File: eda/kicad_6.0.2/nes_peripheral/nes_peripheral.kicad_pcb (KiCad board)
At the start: 2 copper layers, 100 x 100 mm, 111 parts, among them J1 CONN_USER, J11 CONN_JOY2_OE_SEL, J12 CONN_JOY1_OE_SEL, J15 CONN_JOY1_MIC, J16 CONN_5V_RESERVE, J2 CONN_JOY1_FC_COMPATIBLE, J22 CONN_JOY2_MIC, J23 FC_CONN, J24 CONN_CART_DBG, J25 CONN_CART_DBG, J28 CONN_JOY2_DBGSEL, J29 CONN_JOY1_DBGSEL, J3 CONN_JOY2_FC_COMPATIBLE, J30 CONN_GAINSEL, J31 Screw_Terminal_SPK, J33 CONN_JOY2_DBG, J34 CONN_JOY1_DBG, J4 Jack_EXT5V, J7 CONN_CART_OE_SEL, J8 CONN_5VSEL, U1 TXB0104PW, U10 TXB0104PW, U11 TXB0104PW, U12 TXB0104PW, U13 TXB0104PW, U14 TXB0104PW, U15 TXB0104PW, U16 TXB0104PW, U17 4021, U18 4021, U19 MAX98357, U2 TXB0104PW, U3 TXB0104PW, U4 TXB0104PW, U5 TXB0104PW, U6 TXB0104PW, U7 TXB0104PW, U8 TXB0104PW, U9 TXB0104PW

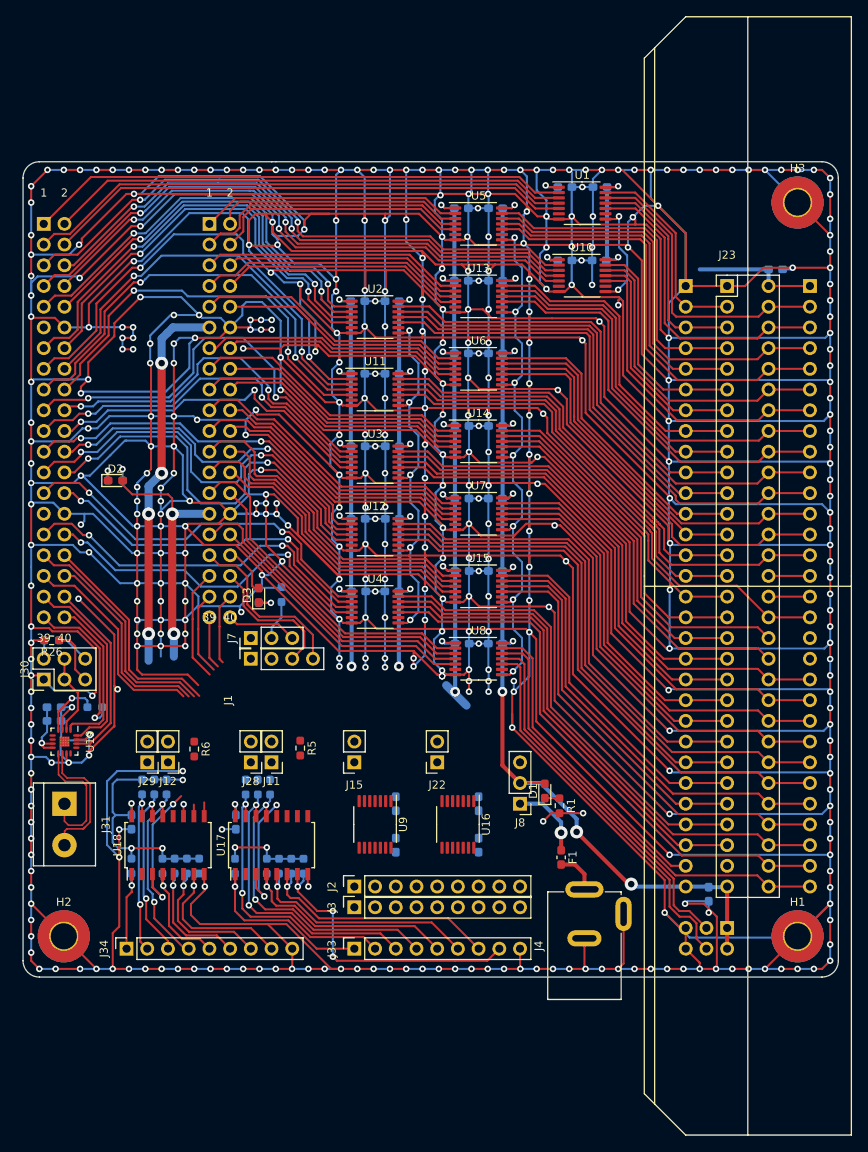
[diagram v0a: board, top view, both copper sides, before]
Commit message: feat: コントローラ用回路を引いた
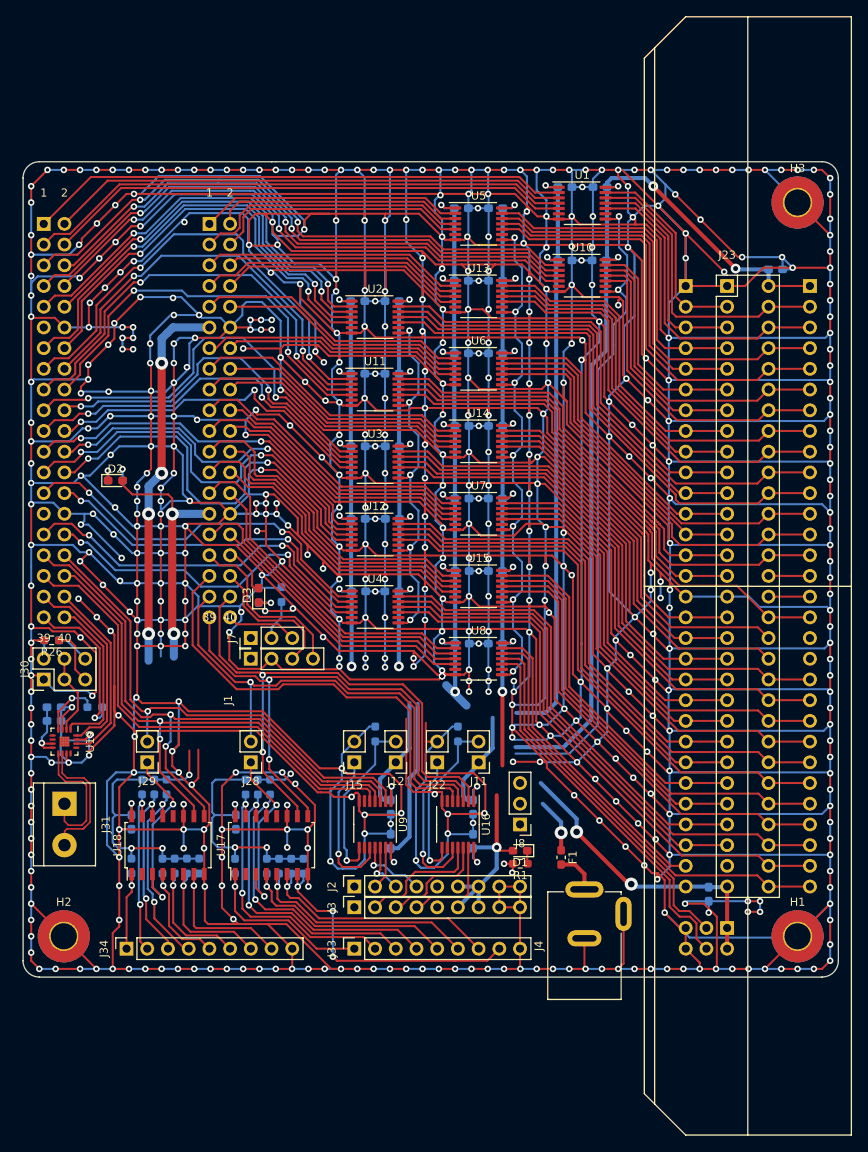
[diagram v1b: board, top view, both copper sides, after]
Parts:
- R5, R6: moved to B.Cu
- moved J12 27.9 mm to (86.4, 116.8)
- moved J11 25.4 mm to (96.5, 116.8)
- moved R6 22.3 mm to (83.8, 113.4), turned to 90 degrees
- moved R5 19.4 mm to (94.0, 113.4), turned to 90 degrees
- moved R1 8.59 mm to (101.6, 129.3), turned to 180 degrees
- moved D1 7.93 mm to (101.6, 127.7), turned to 180 degrees
- moved J8 2.54 mm to (101.6, 124.5)
- moved C33 0.83 mm to (95.8, 126.5)
- moved C28 0.80 mm to (95.8, 122.3)
- moved C21 0.79 mm to (85.7, 126.5)
- moved C13 0.75 mm to (85.7, 122.3)
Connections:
- JP2 pad 35: /3V3_JOY2_DO -> /3V3_JOY2_MICIN
- JP2 pad 37: /3V3_JOY2_MICIN -> /3V3_JOY2_DO
- U16 pad 11: /5V_JOY2_CLK -> /5V_JOY2_DO
- U16 pad 13: /5V_JOY2_DO -> /5V_JOY2_CLK
- U16 pad 2: /3V3_JOY2_DO -> /3V3_JOY2_CLK
- U16 pad 4: /3V3_JOY2_CLK -> /3V3_JOY2_DO
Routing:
- net GND: track 3216.7 -> 3973.7 mm, vias 458 -> 603
- net +3V3: track 244.9 -> 375.3 mm, vias 26 -> 29
- net +5V: track 226.5 -> 355.4 mm, vias 18 -> 23
- net /CART_OE: track 134.2 -> 201.0 mm
- net /3V3_JOY2_CLK: track 8.76 -> 71.1 mm, vias 0 -> 2
- net /3V3_JOY2_P/~{S}: track 6.45 -> 67.8 mm, vias 0 -> 2
- net /3V3_JOY2_DO: track 13.8 -> 60.1 mm, vias 0 -> 1
- net /3V3_JOY2_MICIN: track 10.3 -> 55.5 mm
- net /3V3_JOY1_P/~{S}: track 30.9 -> 75.2 mm, vias 0 -> 2
- net /3V3_JOY1_CLK: track 26.3 -> 69.4 mm, vias 0 -> 2
- net /3V3_JOY1_DO: track 27.3 -> 62.4 mm, vias 0 -> 1
- net /3V3_JOY1_RESERVE: track 26.5 -> 57.9 mm
- net /JOY1_OE_5V: track 0.00 -> 21.8 mm, vias 0 -> 1
- net /JOY2_OE_5V: track 0.00 -> 21.6 mm, vias 0 -> 1
- net /5V_JOY1_RESERVE: track 0.00 -> 18.9 mm, vias 0 -> 1
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
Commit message: feat: 3.3Vを配線
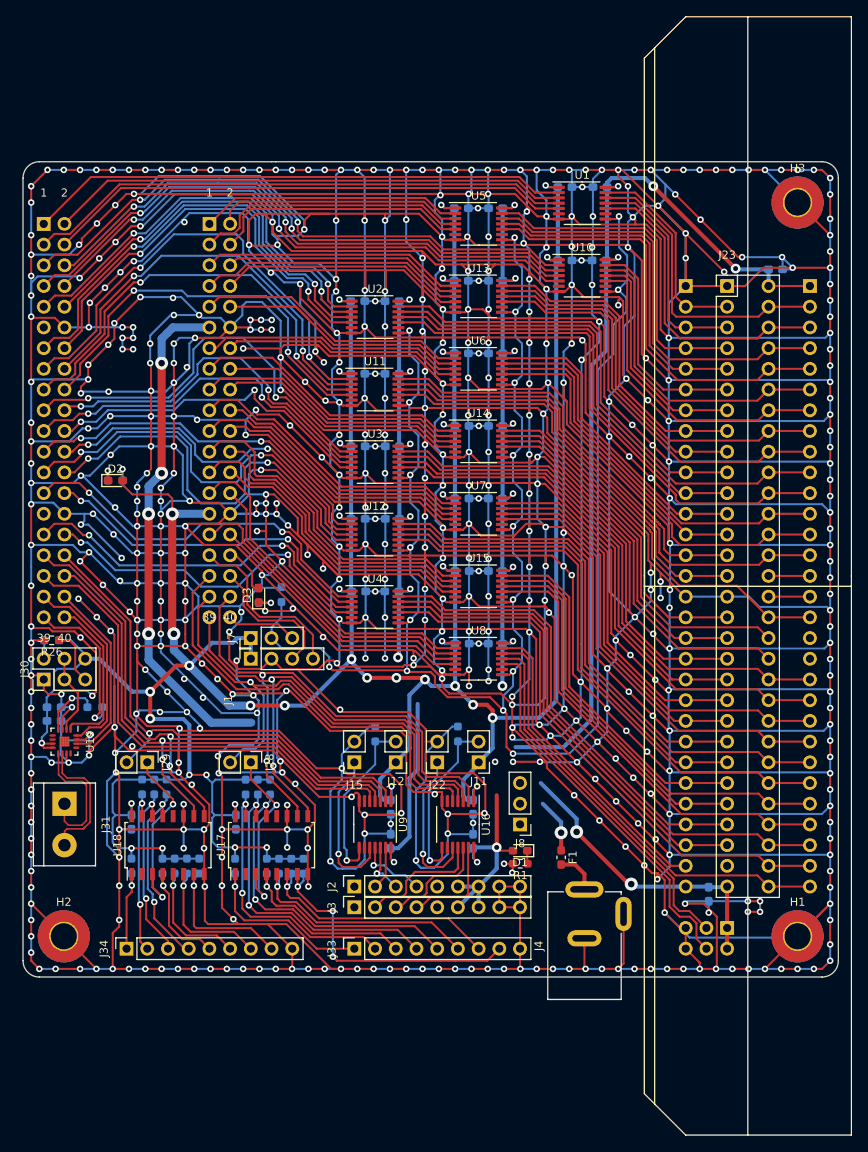
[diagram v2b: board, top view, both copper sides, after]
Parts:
- turned J28 to -90 degrees
- turned J29 to -90 degrees
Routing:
- net GND: track 3973.7 -> 4091.8 mm, vias 603 -> 615
- net +3V3: track 375.3 -> 473.1 mm, vias 29 -> 39
- net /CART_OE: track 201.0 -> 252.2 mm, vias 14 -> 18
- net /BOARD_5V: track 46.8 -> 62.5 mm
- net +5V: track 355.4 -> 344.6 mm
- net /3V3_JOY2_DO: track 60.1 -> 63.9 mm
- net /3V3_JOY1_DO: track 62.4 -> 64.6 mm
- net /3V3_JOY2_CLK: track 71.1 -> 69.0 mm
- net /3V3_JOY2_P/~{S}: track 67.8 -> 65.7 mm
- net /3V3_JOY2_MICIN: track 55.5 -> 53.7 mm
- net /3V3_JOY1_P/~{S}: track 75.2 -> 73.5 mm
- net /3V3_JOY1_RESERVE: track 57.9 -> 59.1 mm
- net /3V3_JOY1_CLK: track 69.4 -> 68.3 mm

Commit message: feat: 配線終わり
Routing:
- net GND: track 4091.8 -> 4256.6 mm, vias 615 -> 692
- net /BOARD_5V: track 62.5 -> 104.7 mm, vias 4 -> 7
- net +5V: track 344.6 -> 382.8 mm, vias 23 -> 25
- net /5V_~{VRAMCS}: track 47.2 -> 52.3 mm
- net /5V_~{PA13}: track 48.0 -> 53.1 mm
- net /5V_PD3: track 38.6 -> 43.6 mm
- net +3V3: track 473.1 -> 474.6 mm, vias 39 -> 35
- net /DAC_I2S_DIN: track 20.6 -> 20.0 mm
- net /5V_JOY2_CLK: track 13.2 -> 12.7 mm
- added copper zone on B.Cu, net GND
- added copper zone on F.Cu, net GND

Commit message: feat: DRC通した
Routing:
- net GND: track 4256.6 -> 4263.4 mm
- net +3V3: track 474.6 -> 475.2 mm
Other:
- board text removed: "39"
- board text removed: "40"

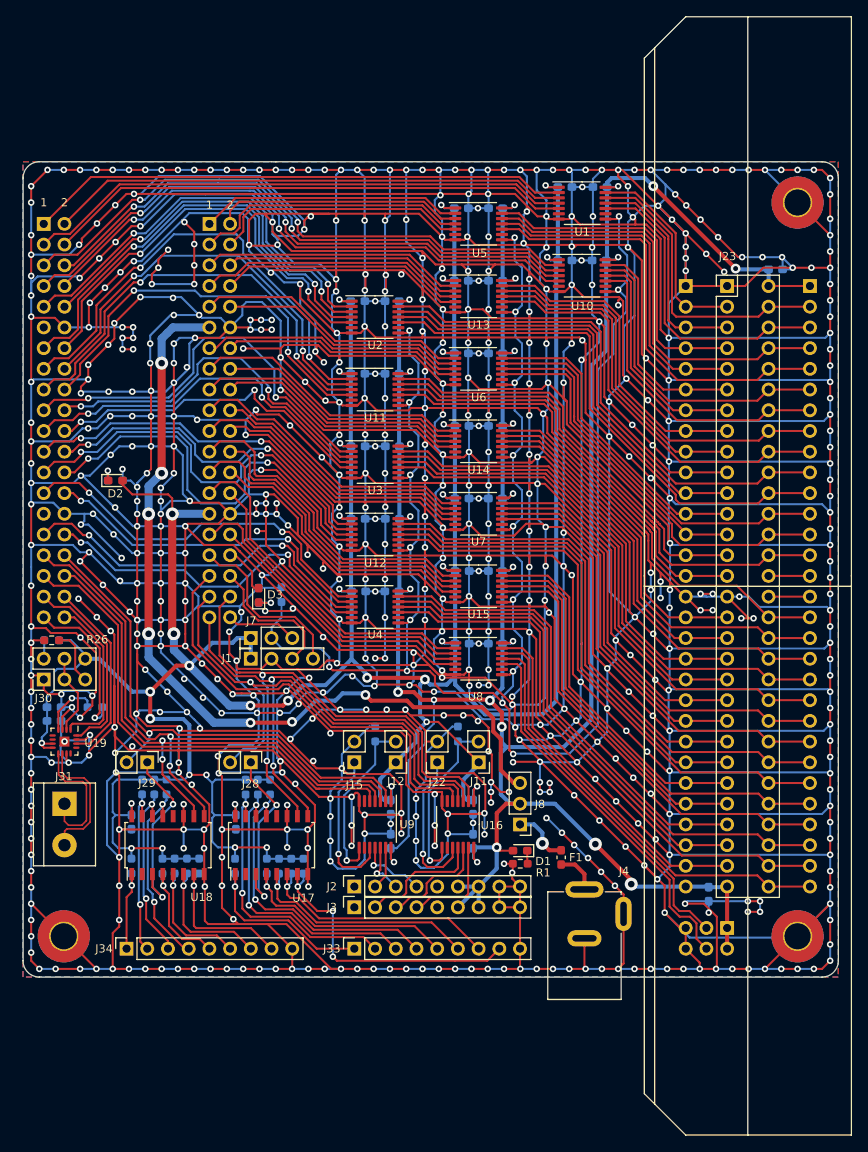
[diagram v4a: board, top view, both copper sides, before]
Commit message: feat: 表面のシルクを整備
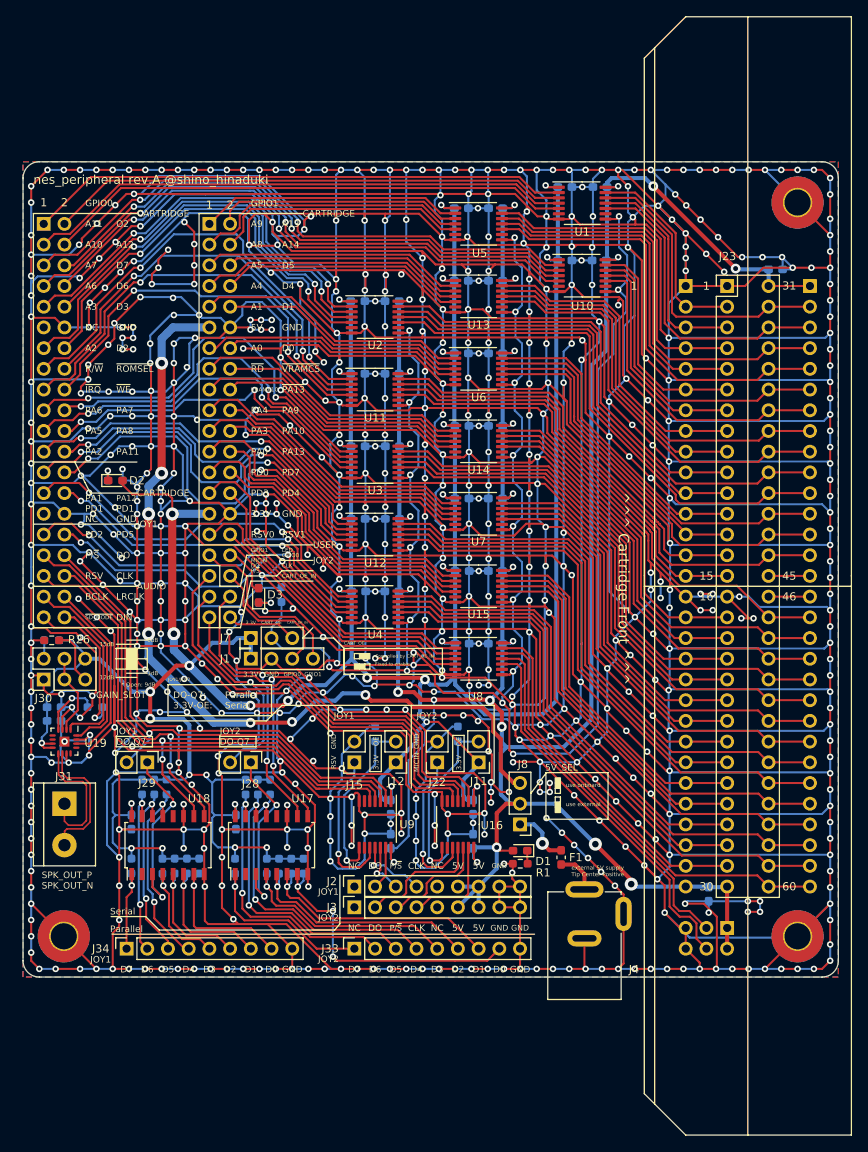
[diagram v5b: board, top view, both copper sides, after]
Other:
- board text added: "* Open: 9dB"
- board text added: "12dB"
- board text added: "15"
- board text added: "15dB"
- board text added: "16"
- board text added: "3.3V"
- board text added: "3.3V-OE:"
- board text added: "30"
- board text added: "31"
- board text added: "3dB"
- board text added: "45"
- board text added: "46"
- board text added: "5V"
- board text added: "5V_SEL"
- board text added: "60"
- board text added: "6dB"
- board text added: "A0"
- board text added: "A1"
- board text added: "A10"
- board text added: "A11"
- board text added: "A12"
- board text added: "A13"
- board text added: "A14"
- board text added: "A2"
- board text added: "A3"
- board text added: "A4"
- board text added: "A5"
- board text added: "A6"
- board text added: "A7"
- board text added: "A8"
- board text added: "A9"
- board text added: "AUDIO"
- board text added: "BCLK"
- board text added: "CARTRIDGE"
- board text added: "CART_OE"
- board text added: "CART_OE_IN"
- board text added: "CLK"
- board text added: "Controlled by CART_OE_IN"
- board text added: "D0"
- board text added: "D1"
- board text added: "D2"
- board text added: "D3"
- board text added: "D4"
- board text added: "D5"
- board text added: "D6"
- board text added: "D7"
- board text added: "DIN"
- board text added: "DO"
- board text added: "DO-Q7:"
- board text added: "Fixed to enable"
- board text added: "GAIN_SLOT"
- board text added: "GND"
- board text added: "GPIO0"
- board text added: "GPIO1"
- board text added: "JOY1"
- board text added: "JOY1 DO-Q7"
- board text added: "JOY1/JOY2"
- board text added: "JOY2"
- board text added: "JOY2 DO-Q7"
- board text added: "LED"
- board text added: "LRCLK"
- board text added: "MICIN"
- board text added: "NC"
- board text added: "O2"
- board text added: "OE"
- board text added: "P/~{S}"
- board text added: "PA0"
- board text added: "PA1"
- board text added: "PA10"
- board text added: "PA11"
- board text added: "PA12"
- board text added: "PA13"
- board text added: "PA2"
- board text added: "PA3"
- board text added: "PA4"
- board text added: "PA5"
- board text added: "PA6"
- board text added: "PA7"
- board text added: "PA8"
- board text added: "PA9"
- board text added: "PD0"
- board text added: "PD1"
- board text added: "PD2"
- board text added: "PD3"
- board text added: "PD4"
- board text added: "PD5"
- board text added: "PD7"
- board text added: "Parallel"
- board text added: "R/~{W}"
- board text added: "RSV"
- board text added: "RSV0"
- board text added: "RSV1"
- board text added: "SPK_OUT_P SPK_OUT_N"
- board text added: "Serial"
- board text added: "USER"
- board text added: "VRAMA10"
- board text added: "^^^ Cartridge Front ^^^"
- board text added: "external 5V supply Tip Center Positive"
- board text added: "nes_peripheral rev.A @shino_hinaduki"
- board text added: "use external"
- board text added: "use onboard"
- board text added: "~{IRQ}"
- board text added: "~{PA13}"
- board text added: "~{RD}"
- board text added: "~{ROMSEL}"
- board text added: "~{SD_MODE}"
- board text added: "~{VRAMCS}"
- board text added: "~{WE}"

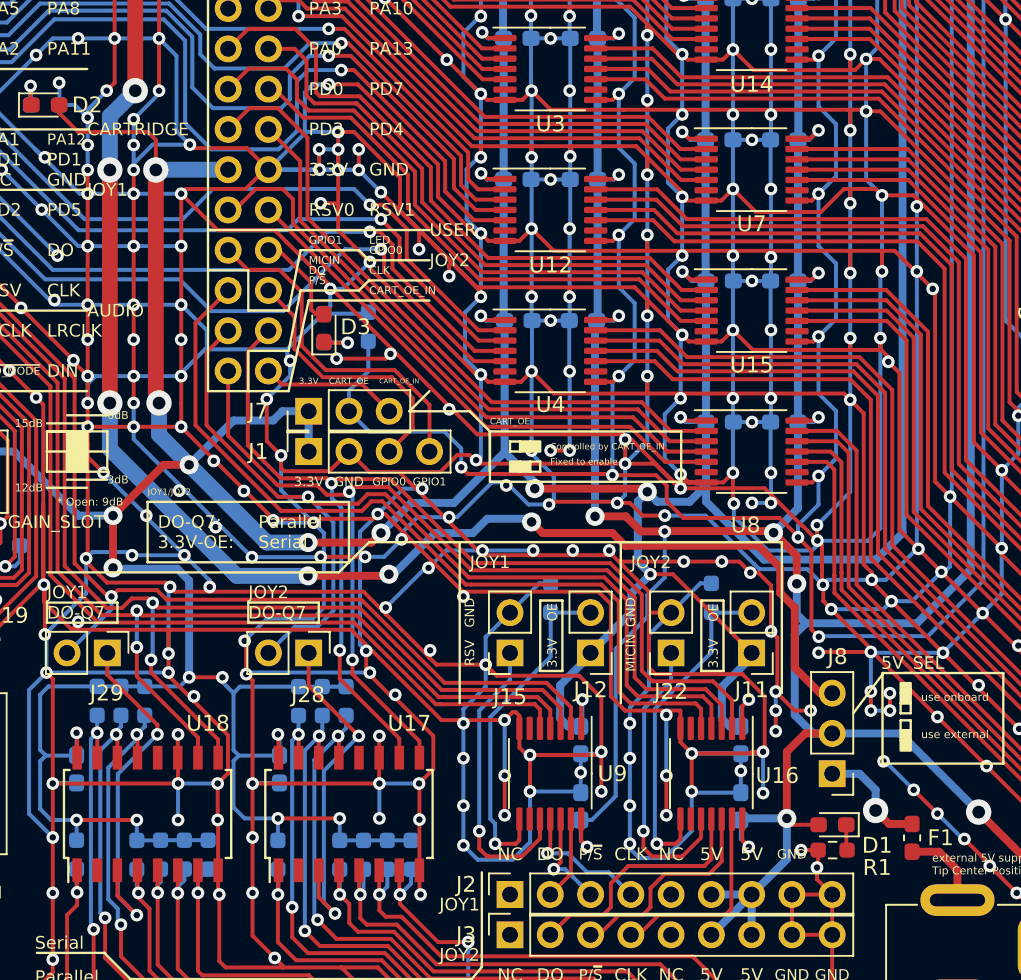
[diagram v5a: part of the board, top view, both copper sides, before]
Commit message: feat: シルク表裏整備
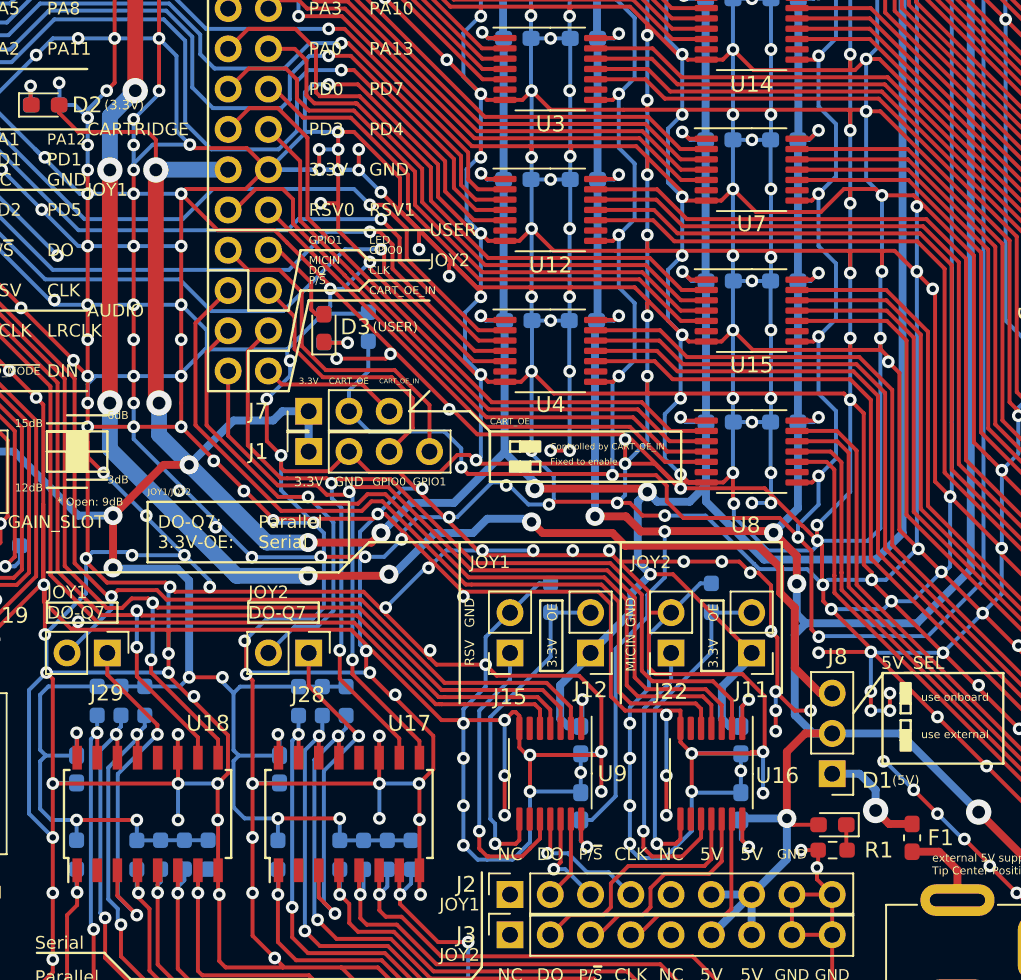
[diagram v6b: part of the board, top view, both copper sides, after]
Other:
- board text added: "(3.3V)"
- board text added: "(5V)"
- board text added: "(USER)"
- board text added: "PD6"
- board text added: "SOUND_I"
- board text added: "SOUND_O"
- board text added: "https://github.com/shino-hinaduki/chisel-nes"
